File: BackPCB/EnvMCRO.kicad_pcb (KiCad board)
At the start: 2 copper layers, 109.6 x 69.7 mm, 4 parts

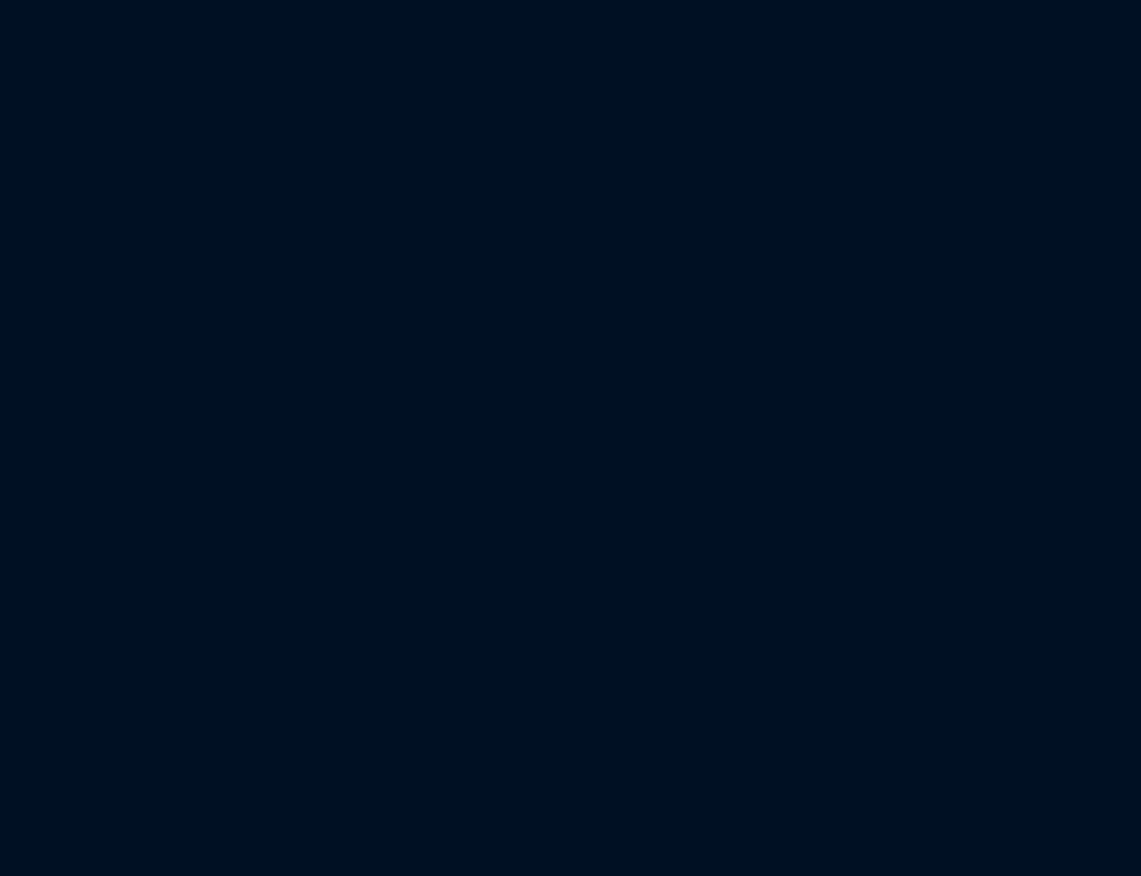
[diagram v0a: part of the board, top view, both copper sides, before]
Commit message: Added logo to back plate
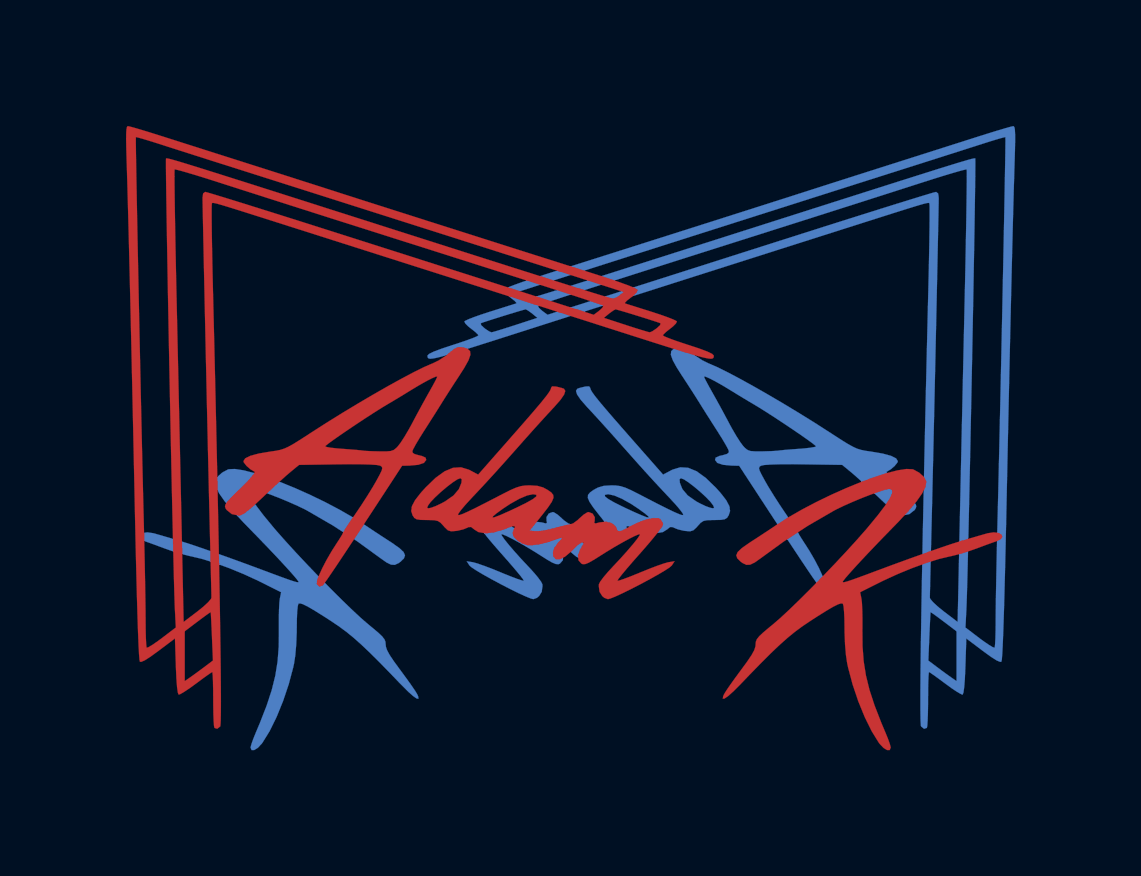
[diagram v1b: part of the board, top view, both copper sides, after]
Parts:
- added G***: LOGO, Logo:logoLarge, B.Cu at (118.2, 73.7)
- added G***: LOGO, Logo:logoLarge, F.Cu at (118.2, 73.7)

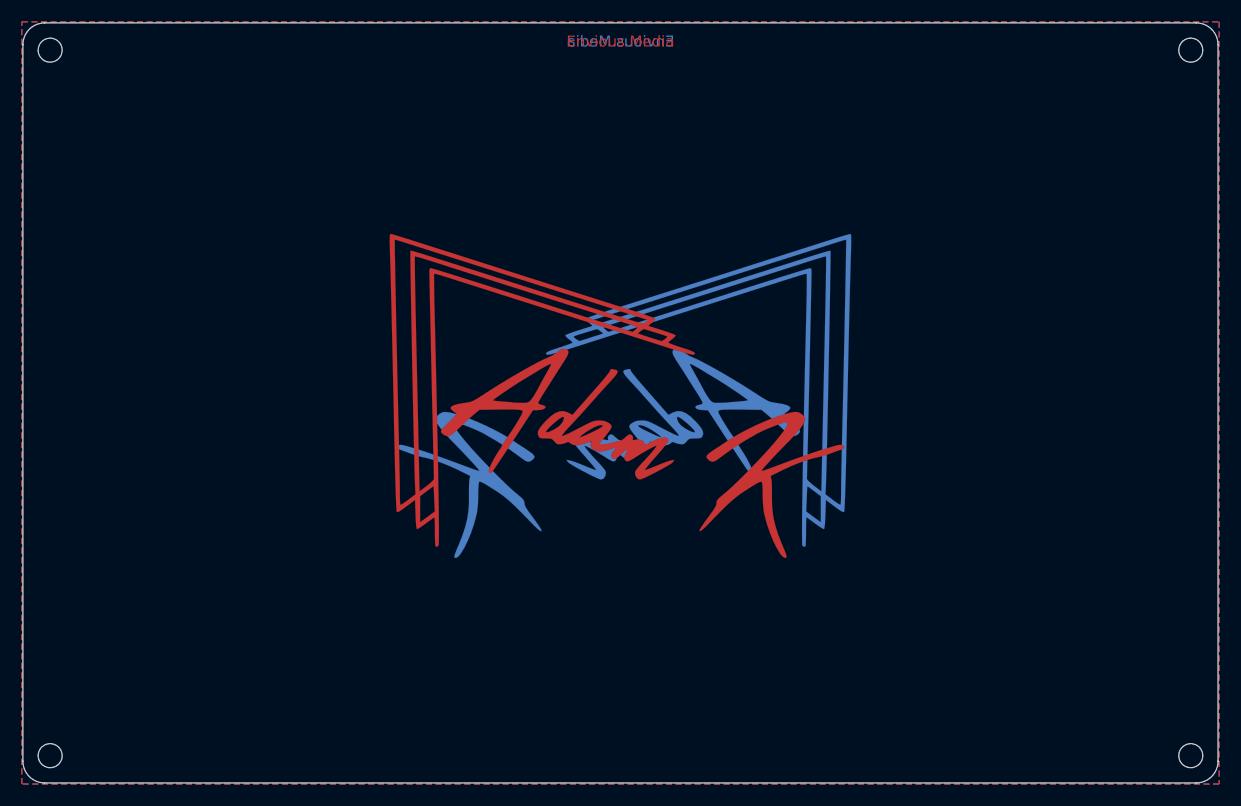
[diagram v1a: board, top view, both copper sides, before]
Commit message: updated macro boards to have padded mount holes and github url
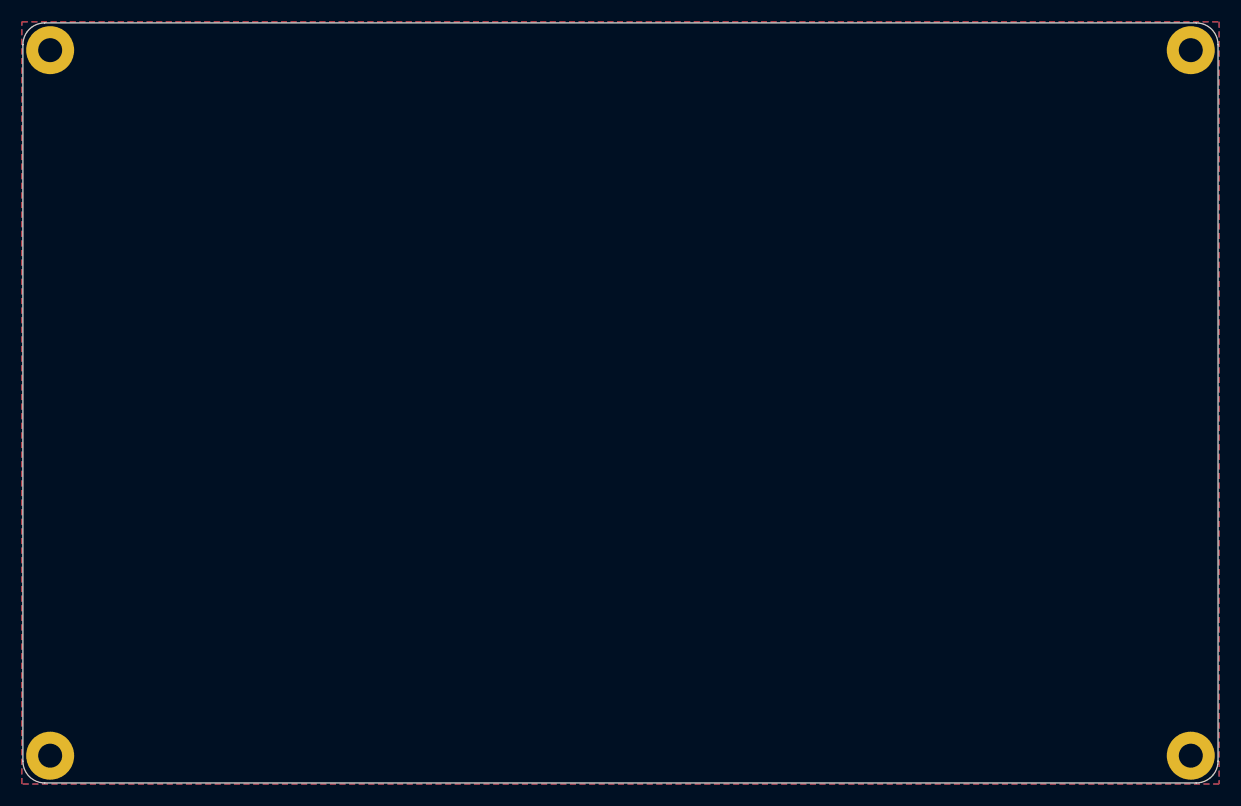
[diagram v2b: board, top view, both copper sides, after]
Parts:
- H1, H2, H3, H4: footprint MountingHole:MountingHole_2.2mm_M2 -> MountingHole:MountingHole_2.2mm_M2_Pad
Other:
- board text removed: "Envious.Media"
